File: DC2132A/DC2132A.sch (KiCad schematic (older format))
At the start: 5 parts, among them U3 LT8612

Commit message: new kicad version
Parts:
- removed C3: 10uF, ~, symbol C
- removed C8: 22uf, ~, symbol CP1
- removed R5: 499k, ~, symbol R
- removed R6: 54.9k, ~, symbol R
- added C3: 10uF, TO_SOT_Packages_SMD:TO-50-3_LongPad-NoHole_Housing, symbol C_Small
- added C8: 22uF, Power_Integrations:TO-263-7C, symbol CP1_Small
- added D1: LED, LEDs:LED-3MM, symbol LED
- added R1, R2: R_Small, Resistors_SMD:R_0603, symbol R_Small
- added R5: 499k, Resistors_SMD:R_0603, symbol R_Small
- added R6: 54.9k, Resistors_SMD:R_0603, symbol R_Small
- added RV1: POT, Potentiometers:Potentiometer_Spectrol-Type148-Type149_Single, symbol POT
- added U1, U2: LT3081, symbol LT3081
- added U4: LT3092, Housings_DFN_QFN:DFN-8-1EP_3x3mm_Pitch0.5mm, symbol LT3092
- U3: footprint ~ -> Housings_DFN_QFN:QFN-28-1EP_3x6mm_Pitch0.5mm
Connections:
- net labels added: INVCC
- wire segments 14 -> 13
- no-connect marks 16 -> 0
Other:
- moved on the sheet: U3

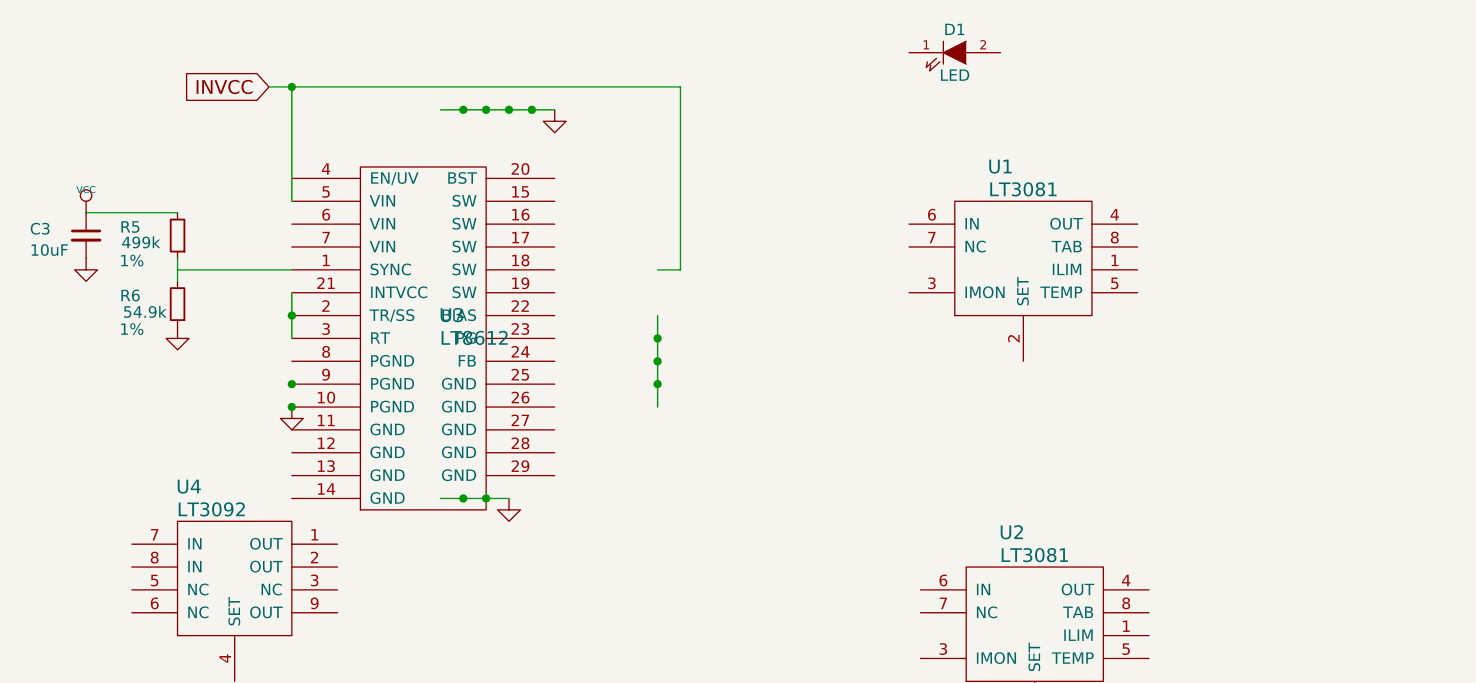
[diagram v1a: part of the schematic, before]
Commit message: added more components from lt schematic
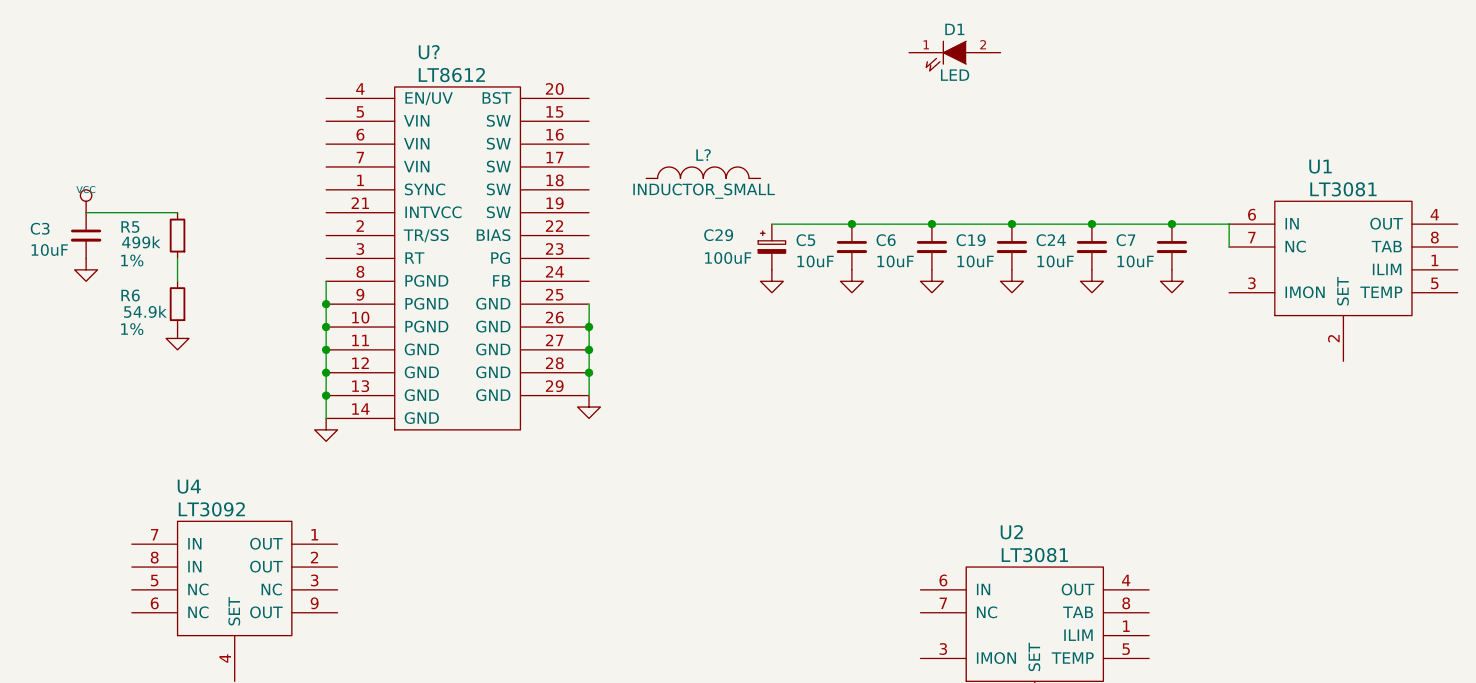
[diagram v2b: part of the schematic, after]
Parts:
- removed U3: LT8612, Housings_DFN_QFN:QFN-28-1EP_3x6mm_Pitch0.5mm, symbol LT8612
- added C19, C24, C5, C6, C7: 10uF, Capacitors_SMD:C_1210, symbol C_Small
- added C29: 100uF, Capacitors_SMD:c_elec_6.3x7.7, symbol CP_Small
- added L?: INDUCTOR_SMALL, symbol INDUCTOR_SMALL
- added U?: LT8612, symbol LT8612
- C3: footprint TO_SOT_Packages_SMD:TO-50-3_LongPad-NoHole_Housing -> Capacitors_SMD:C_1210
- C8: footprint Power_Integrations:TO-263-7C -> Capacitors_SMD:c_elec_6.3x7.7
- U1, U2: footprint (none) -> DC2132A:TO-263-8
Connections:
- net labels removed: INVCC
- wire segments 13 -> 8
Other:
- moved on the sheet: U1
